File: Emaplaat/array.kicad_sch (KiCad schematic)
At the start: 36 parts, among them IC2 1EDN7550BXTSA1, IC3 1EDN7550BXTSA1, IC4 1EDN7550BXTSA1, IC5 1EDN7550BXTSA1, IC6 1EDN7550BXTSA1, IC7 1EDN7550BXTSA1, IC8 1EDN7550BXTSA1, U1 1EDN7550BXTSA1

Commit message: ketamine addict
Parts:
- removed C11, C14, C16, C18: 100u, symbol Device:C
- removed C13, C15, C17, C19: 20u, Capacitor_SMD:C_0201_0603Metric, symbol Device:C
- removed IC5, IC6, IC7, IC8: 1EDN7550BXTSA1, SOT95P280X145-6N, symbol 1EDN7550BXTSA1:1EDN7550BXTSA1
- removed R10, R11, R12, R13, R14, R15, R16, R17, R5: 33k, symbol Device:R
- added C100, C172, C175, C222: 100u, Capacitor_SMD:C_0201_0603Metric_Pad0.64x0.40mm_HandSolder, symbol Device:C
- added C170, C173, C221, C99: 20u, Capacitor_SMD:C_0603_1608Metric_Pad1.08x0.95mm_HandSolder, symbol Device:C
- added IC103, IC42, IC78, IC79: 1EDN7550BXTSA1, SOT95P280X145-6N, symbol 1EDN7550BXTSA1:1EDN7550BXTSA1
- added R117, R118, R119, R120, R161, R162, R64, R65, R69: 33k, Resistor_SMD:R_0603_1608Metric_Pad0.98x0.95mm_HandSolder, symbol Device:R
- C10, C7: value 100u -> 20u; footprint (none) -> Capacitor_SMD:C_0603_1608Metric_Pad1.08x0.95mm_HandSolder
- C12, C9: value 20u -> 100u; footprint Capacitor_SMD:C_0201_0603Metric -> Capacitor_SMD:C_0201_0603Metric_Pad0.64x0.40mm_HandSolder
- C6: footprint (none) -> Capacitor_SMD:C_0201_0603Metric_Pad0.64x0.40mm_HandSolder
- C8: footprint Capacitor_SMD:C_0805_2012Metric_Pad1.18x1.45mm_HandSolder -> Capacitor_SMD:C_0603_1608Metric_Pad1.08x0.95mm_HandSolder
- R4: footprint Resistor_SMD:R_0603_1608Metric -> Resistor_SMD:R_0603_1608Metric_Pad0.98x0.95mm_HandSolder
- R6, R7, R8, R9: footprint (none) -> Resistor_SMD:R_0603_1608Metric_Pad0.98x0.95mm_HandSolder
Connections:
- net 12V: now also C12.2, C6.2, C9.2, C100.2, C172.2, C175.2, C222.2, IC103.4 (VDD), IC42.4 (VDD), IC78.4 (VDD), IC79.4 (VDD); no longer C10.1, C6.1, C7.1
- net 1A+: now also R69.2
- net 1C+: now also R65.2
- net 1C-: now also R64.2
- net 1D+: now also R120.2
- net 1D-: now also R119.2
- net 1E+: now also R162.2
- net 1E-: now also R161.2
- net 1G+: now also R118.2
- net 1G-: now also R117.2
- net FLIXEL_B: now also C10.2; no longer C12.2
- net FLIXEL_C: now also C99.2
- net FLIXEL_D: now also C173.2
- net FLIXEL_E: now also C221.2
- net FLIXEL_F: now also C7.2; no longer C9.2
- net FLIXEL_G: now also C170.2
- net PGND: now also C12.1, C6.1, C9.1, C100.1, C172.1, C175.1, C222.1, IC103.2 (GND), IC42.2 (GND), IC78.2 (GND), IC79.2 (GND); no longer C10.2, C6.2, C7.2
- net at IC3.5 (OUT_SRC), IC3.6 (OUT_SNK): now also C7.1; no longer C9.1
- net at IC2.3 (IN+): now also R69.1
- net at IC4.5 (OUT_SRC), IC4.6 (OUT_SNK): now also C10.1; no longer C12.1
- new net: IC79.1 (IN-), R119.1
- new net: IC42.3 (IN+), R65.1
- new net: IC103.3 (IN+), R162.1
- new net: C99.1, IC42.5 (OUT_SRC), IC42.6 (OUT_SNK)
- new net: C170.1, IC78.5 (OUT_SRC), IC78.6 (OUT_SNK)
- new net: IC103.1 (IN-), R161.1
- new net: C221.1, IC103.5 (OUT_SRC), IC103.6 (OUT_SNK)
- new net: IC42.1 (IN-), R64.1
- new net: IC79.3 (IN+), R120.1
- new net: IC78.3 (IN+), R118.1
- new net: IC78.1 (IN-), R117.1
- new net: C173.1, IC79.5 (OUT_SRC), IC79.6 (OUT_SNK)
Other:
- moved on the sheet: C6, C8, IC2, U1

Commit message: T________T Heiki Tammemägi
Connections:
- net PGND renamed GND
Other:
- moved on the sheet: C10, C12, C170, C172, C173, C175, C221, C222, C6, C7, C8, C9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

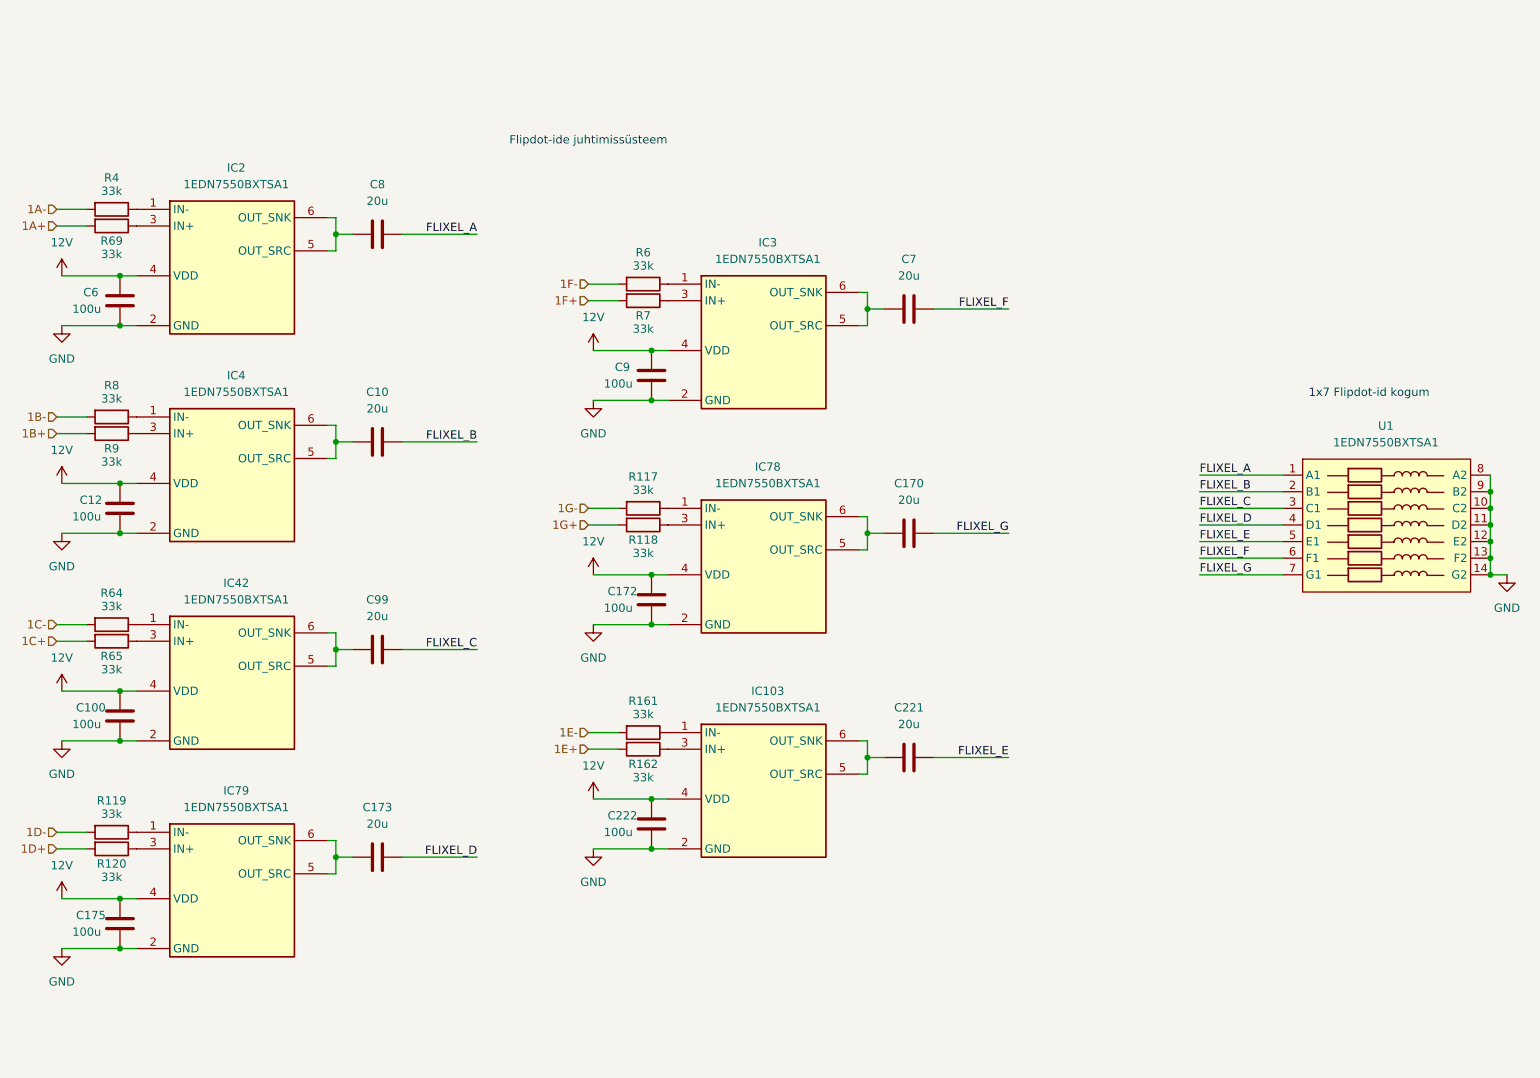
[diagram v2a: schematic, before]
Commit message: skeem v2 kinda valmis, simulatsioon ka tehtud
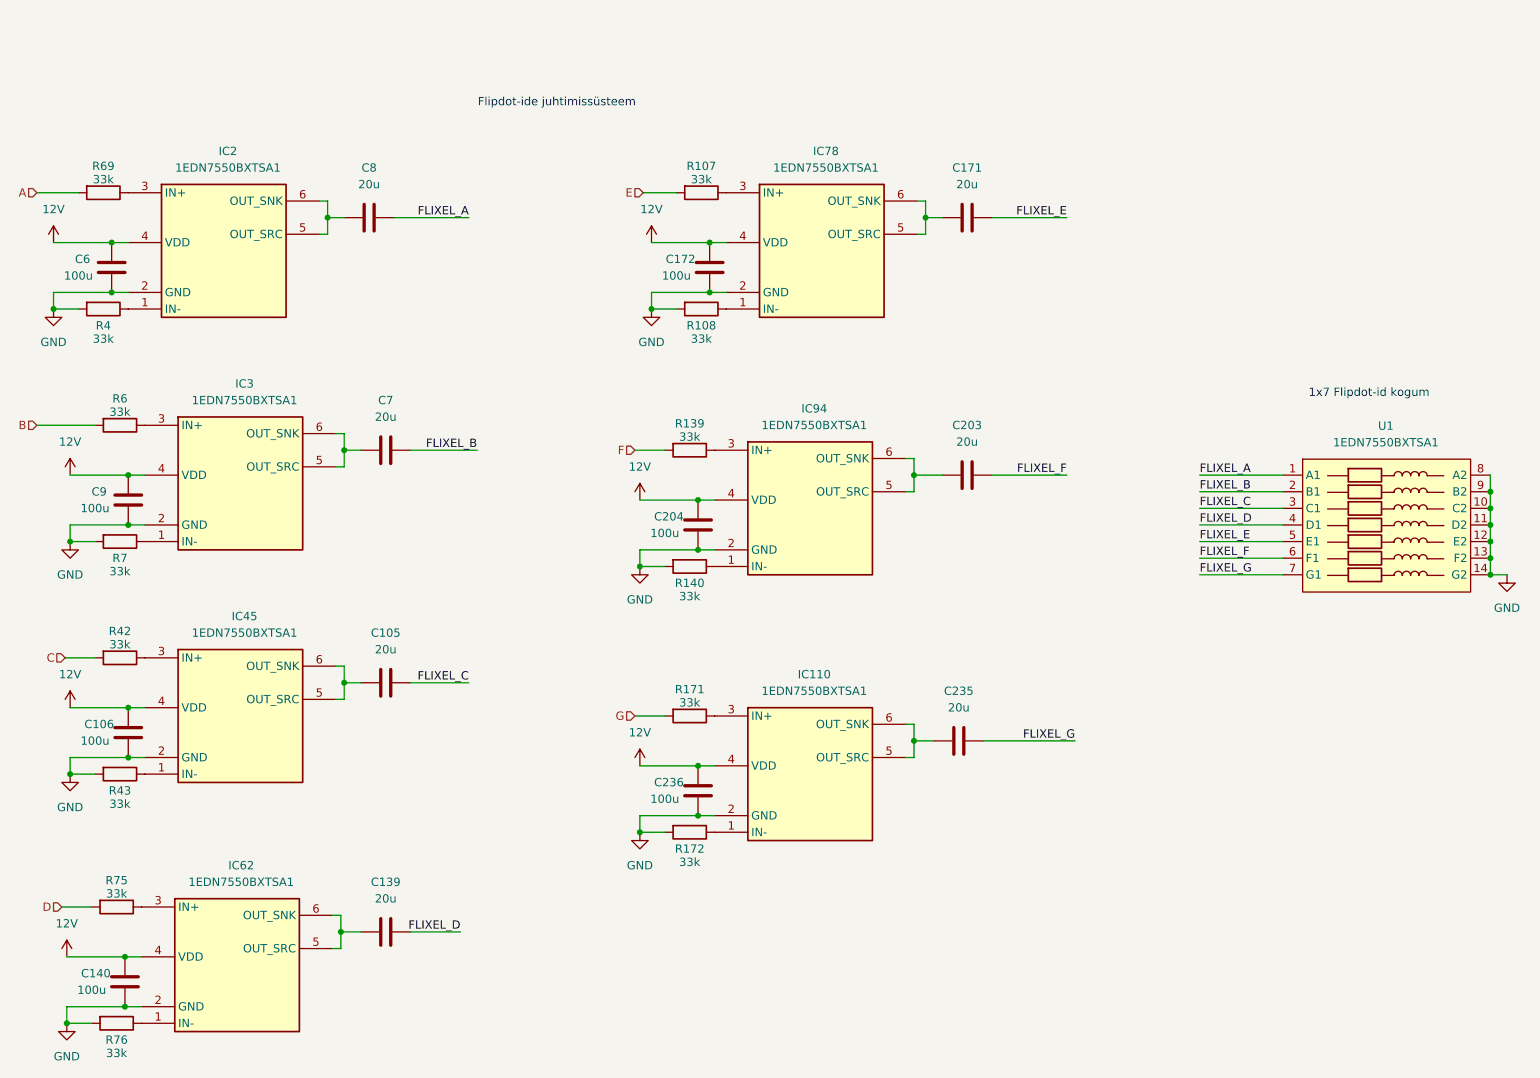
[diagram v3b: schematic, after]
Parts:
- removed C10, C170, C173, C221, C99: 20u, Capacitor_SMD:C_0603_1608Metric_Pad1.08x0.95mm_HandSolder, symbol Device:C
- removed C100, C12, C175, C222: 100u, Capacitor_SMD:C_0201_0603Metric_Pad0.64x0.40mm_HandSolder, symbol Device:C
- removed IC103, IC4, IC42, IC79: 1EDN7550BXTSA1, SOT95P280X145-6N, symbol 1EDN7550BXTSA1:1EDN7550BXTSA1
- removed R117, R118, R119, R120, R161, R162, R64, R65, R8, R9: 33k, Resistor_SMD:R_0603_1608Metric_Pad0.98x0.95mm_HandSolder, symbol Device:R
- added C105, C139, C171, C203, C235: 20u, Capacitor_SMD:C_0603_1608Metric_Pad1.08x0.95mm_HandSolder, symbol Device:C
- added C106, C140, C204, C236: 100u, Capacitor_SMD:C_0201_0603Metric_Pad0.64x0.40mm_HandSolder, symbol Device:C
- added IC110, IC45, IC62, IC94: 1EDN7550BXTSA1, SOT95P280X145-6N, symbol 1EDN7550BXTSA1:1EDN7550BXTSA1
- added R107, R108, R139, R140, R171, R172, R42, R43, R75, R76: 33k, Resistor_SMD:R_0603_1608Metric_Pad0.98x0.95mm_HandSolder, symbol Device:R
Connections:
- net 1A- is gone; now on net GND: R4.2
- net 1F+ is gone; now on net GND: R7.2
- net 12V: now also C106.2, C140.2, C204.2, C236.2, IC110.4 (VDD), IC45.4 (VDD), IC62.4 (VDD), IC94.4 (VDD)
- net FLIXEL_B: now also C7.2
- net FLIXEL_C: now also C105.2
- net FLIXEL_D: now also C139.2
- net FLIXEL_E: now also C171.2
- net FLIXEL_F: now also C203.2; no longer C7.2
- net FLIXEL_G: now also C235.2
- net GND: now also C106.1, C140.1, C204.1, C236.1, IC110.2 (GND), IC45.2 (GND), IC62.2 (GND), IC94.2 (GND), R108.2, R140.2, R172.2, R43.2, R76.2
- net at IC78.5 (OUT_SRC), IC78.6 (OUT_SNK): now also C171.1
- net at IC3.3 (IN+): now also R6.1; no longer R7.1
- net at IC78.3 (IN+): now also R107.1
- net at IC78.1 (IN-): now also R108.1
- net at IC3.1 (IN-): now also R7.1; no longer R6.1
- net 1A+ renamed A
- net 1F- renamed B
- new net: IC62.3 (IN+), R75.1
- new net: IC94.1 (IN-), R140.1
- new net: IC94.3 (IN+), R139.1
- new net: C203.1, IC94.5 (OUT_SRC), IC94.6 (OUT_SNK)
- new net: C235.1, IC110.5 (OUT_SRC), IC110.6 (OUT_SNK)
- new net: C139.1, IC62.5 (OUT_SRC), IC62.6 (OUT_SNK)
- new net: C105.1, IC45.5 (OUT_SRC), IC45.6 (OUT_SNK)
- new net: IC45.1 (IN-), R43.1
- new net: IC45.3 (IN+), R42.1
- new net: IC110.1 (IN-), R172.1
- new net: IC110.3 (IN+), R171.1
- new net: IC62.1 (IN-), R76.1
- new net C: R42.2
- new net D: R75.2
- new net E: R107.2
- new net F: R139.2
- new net G: R171.2
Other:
- moved on the sheet: C6, C8, IC2, R4, R69
